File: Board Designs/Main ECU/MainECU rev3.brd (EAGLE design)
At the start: 120.6 x 78.9 mm, 155 parts, among them Q1 MMBT3904LT3G, Q11 MMBT3904LT3G, Q2 MMBT3904LT3G, Q3 MMBT3904LT3G, Q4 MMBT3904LT3G, Q5 MMBT3904LT3G, Q6 MMBT3904LT3G, Q7 MMBT3904LT3G, Q8 MMBT3904LT3G, Q9 MMBT3904LT3G, X1 CONNECTOR-37, X2 CONNECTOR-4AUTOSPORT, X3 CONNECTOR-4NANO-FIT-VERTICAL-4, X4 CONNECTOR-4NANO-FIT-VERTICAL-4

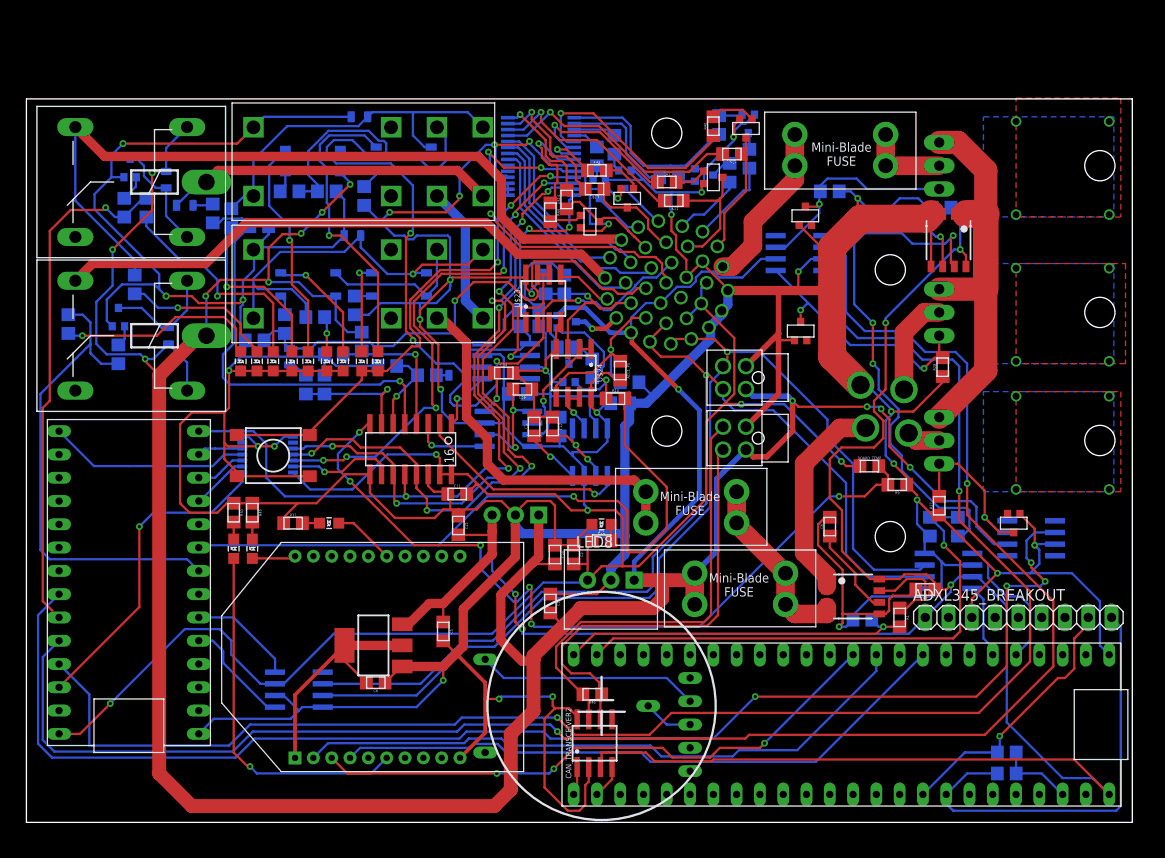
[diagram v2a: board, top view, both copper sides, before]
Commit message: Rename Main ECU rev1b -> rev3, rev3 -> rev4
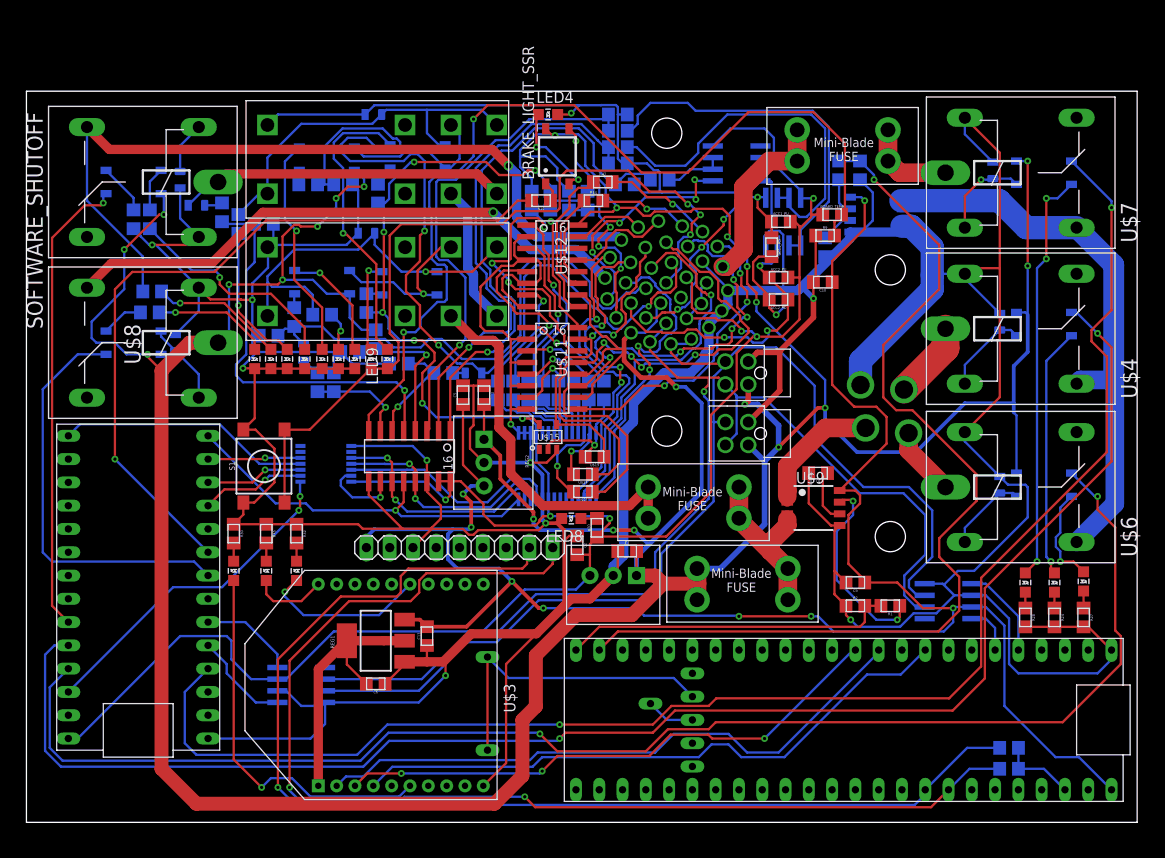
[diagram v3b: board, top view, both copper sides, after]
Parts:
- removed C14, C17: 47pF, HyTechDevices:0805
- removed C15, C16, C18, C19, C21: .1uF, HyTechDevices:0805
- removed C20: .22uF, HyTechDevices:0805
- removed CAN_TRANSCEIVER2: MCP2551, HyTechDevices:SOIC-08
- removed Q1, Q11, Q2, Q3, Q4, Q5, Q6, Q7, Q8, Q9: MMBT3904LT3G, HyTechDevices:SOT23
- removed Q10: (no value), HyTechDevices:SOT23
- removed R46: 120, HyTechDevices:0805
- removed R47, R50: 2.2k, HyTechDevices:0805
- removed R48: 10k, HyTechDevices:0805
- removed R49: 1.2k, HyTechDevices:0805
- removed REG3: 5V, HyTechDevices:OKI-78SR
- removed U$27, U$28: (no value), HyTechDevices:SOIC-08
- added AC1_FILTR, AC2_FILTR: 510, HyTechDevices:0805
- added BRAKE_LIGHT_SSR, FAN_SSR1, FAN_SSR2, INVERTER_SSR, PUMP_SSR: CPC1002N, HyTechDevices:SOP04
- added BR_FILTR: 100, HyTechDevices:0805
- added C13: .1uF, HyTechDevices:0805
- added LED12, LED13, LED16, LED4: Red, HyTechDevices:LED-805
- added R25: 330, HyTechDevices:0805
- added REG2: 5V, HyTechDevices:OKI-78SR
- added U$20, U$21, U$22: JUMPER, HyTechDevices:0805
- C11: value (none) -> .22uF
- C12: value .1uF -> 2.2µ
- C3: value 47pF -> 22µ
- C4: value .1uF -> 22µ
- D7, D8, D9: value MMBZ5246BLT1G -> DIODE0805; device HyTechDevices:SOT23 -> HyTechDevices:0805_D
- R10: value 2.2k -> 43
- R16: value 100 -> 43
- R24, R27, R28: value 10k -> 33
- R35, R36, R38, R39, R40, R41, R42: value 2.2k -> 270
- R37: value 0 -> 270
- R44: value 2.2k -> 0
- U$11, U$12: value JUMPER -> TLP291-4; device HyTechDevices:0805 -> HyTechDevices:SOIC-16
- U$15: value BJT_PNPSOT -> SN74LV1T34; device HyTechDevices:SOT23 -> HyTechDevices:SOT-23-5
- U$16: value CR-2450/G1AN -> JUMPER; device HyTechDevices:CR-2450/G1AN -> HyTechDevices:0805
- U$19: value MC34152 -> JUMPER; device HyTechDevices:SOIC-08 -> HyTechDevices:0805
- U$26: value (none) -> CR-2450/G1AN; device HyTechDevices:SOIC-08 -> HyTechDevices:CR-2450/G1AN
- U$4, U$6, U$7: value N-CHANNEL_MOSFET_FQP30N06L -> G5LE; device HyTechDevices:TO-220-H-HOLE -> HyTechDevices:ZF112
- U$5: value MC34152 -> CPC1002N; device HyTechDevices:SOIC-08 -> HyTechDevices:SOP04
- moved U$5 73.1 mm to (11.7, 69.8), turned to 90 degrees
- moved ADXL345_BREAKOUT 61.4 mm to (46.0, 30.0)
- moved U$16 55.2 mm to (59.2, 67.8), flipped to the bottom, turned to 270 degrees
- moved R24 52.5 mm to (112.1, 22.4), flipped to the top, turned to 270 degrees
- moved U$19 48.4 mm to (62.0, 39.9), flipped to the top, turned to 180 degrees
- moved R3 41.0 mm to (88.6, 71.1)
- moved R4 39.6 mm to (90.9, 71.1)
- moved U$26 38.8 mm to (63.0, 13.0)
- moved R35 37.7 mm to (51.4, 47.1)
- moved C3 35.2 mm to (64.5, 77.2), flipped to the bottom, turned to 180 degrees
- moved U$17 33.8 mm to (57.9, 38.9), turned to 0 degrees
- moved U$13 33.0 mm to (60.7, 36.1)
- moved R40 32.6 mm to (59.7, 47.1), flipped to the bottom
- moved R37 32.4 mm to (54.7, 47.1), turned to 90 degrees
- moved U$14 30.0 mm to (60.7, 38.0), turned to 180 degrees
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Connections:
- removed net DASH_CTRL5_IN: U$12.2, U$17.25
- removed net DASH_CTRL5_OUT: R40.1, U$17.5
- removed net DASH_CTRL6_IN: U$11.2, U$17.26
- removed net DASH_CTRL6_OUT: R41.1, U$17.6
- removed net DASH_CTRL7_IN: U$13.2, U$17.27
- removed net DASH_CTRL7_OUT: R42.1, U$17.7
- removed net DASH_CTRL8_IN: U$14.2, U$17.28
- removed net DASH_CTRL8_OUT: R44.1, U$17.8
- removed net FAN1CONTROL: U$1.A8, U$5.2
- removed net FAN1DRIVE: D8.3, R24.2, U$5.7, U$7.1
- removed net FAN2CONTROL: U$1.A9, U$5.4
- removed net FAN2DRIVE: D7.3, R28.2, U$4.1, U$5.5
- removed net N$66: D4.A, Q9.3, U$8.2
- removed net PUMPCONTROL: U$1.A6, U$19.2
- removed net PUMPDRIVE: D9.3, R27.2, U$19.7, U$6.1
- removed net TELEMETRY_CANH: CAN_TRANSCEIVER2.7, R46.2, X4.P$4
- removed net TELEMETRY_CANL: CAN_TRANSCEIVER2.6, R46.1, X4.P$3
- new net DASH_CTRL5: R39.1, U$17.25
- new net DASH_CTRL6: R40.1, U$13.2, U$17.26
- new net DASH_CTRL7: R41.1, U$14.2, U$17.27
- new net DASH_CTRL8: R42.1, U$15.2, U$17.28, U$19.2
- new net N$20: D8.C, FAN_SSR1.3, U$7.2
- new net N$39: FAN_SSR2.2, LED16.A
- new net N$43: D10.C, R26.1, SOFTWARE_SHUTOFF.2, U$5.3
- new net N$44: R25.2, U$5.2
- new net RELAY_CTRL1: PUMP_SSR.1, U$1.A9
- new net RELAY_CTRL2: FAN_SSR1.1, U$1.D2
- new net RELAY_CTRL3: FAN_SSR2.1, U$1.A8
- net +12V: now also BRAKE_LIGHT_SSR.4, C11.2, FAN_SSR1.4, FAN_SSR2.4, INVERTER_SSR.4, PUMP_SSR.4, REG2.1, U$11.10, U$11.12, U$12.10, U$12.12, U$12.14, U$12.16, U$16.1, U$21.1, U$5.4; no longer C20.2, D10.C, D4.C, R48.1, REG3.1, SOFTWARE_SHUTOFF.2, U$15.2, U$19.6, U$5.6, U$8.1
- net +5V: now also U$15.5, U$20.1, U$22.1; no longer C11.2, C15.1, C18.1, C4.1, U$26.4, U$26.7, U$27.4, U$27.7, U$28.4, U$28.7
- net BRAKE_LIGHT: now also BRAKE_LIGHT_SSR.3; no longer U$15.3
- net CANH: now also X4.P$4
- net CANL: now also X4.P$3
- net CURRENTSENSE2: now also U$4.S, U$6.S, U$7.S; no longer U$4.3, U$6.3, U$7.3
- net DASH_CTRL1: now also U$17.21; no longer U$17.1
- net DASH_CTRL10: now also U$17.2; no longer U$17.22
- net DASH_CTRL11: now also U$17.3; no longer U$17.23
- net DASH_CTRL12: now also U$17.4; no longer U$17.24
- net DASH_CTRL2: now also U$17.22; no longer U$17.2
- net DASH_CTRL3: now also R37.1, U$17.23; no longer R38.1, U$17.3
- net DASH_CTRL4: now also R38.1, U$17.24; no longer R39.1, U$17.4
- net DASH_CTRL9: now also U$17.1; no longer U$17.21
- net DASH_IO2: now also R44.2; no longer R37.2
- net DASH_IO3: now also U$12.13; no longer Q3.3
- net DASH_IO4: now also U$12.15; no longer Q4.3
- net DASH_IO5: now also U$11.9; no longer Q5.3, U$12.1
- net DASH_IO6: now also U$11.11, U$13.1; no longer Q6.3, U$11.1
- net DASH_IO7: now also U$11.13, U$14.1; no longer Q7.3, U$13.1
- net DASH_IO8: now also U$11.15, U$15.4, U$19.1; no longer Q8.3, U$14.1
- net FAN1-: now also U$7.P; no longer U$7.2
- net FAN2-: now also U$4.P; no longer U$4.2
- net GND: now also C13.1, D10.A, D4.A, D7.A, D8.A, D9.A, LED4.C, R24.2, R25.1, R27.2, R28.2, REG2.2, SOFTWARE_SHUTOFF.1, U$11.2, U$11.4, U$11.6, U$11.8, U$12.2, U$12.4, U$12.6, U$12.8, U$15.3, U$4.1, U$6.1, U$7.1, U$8.2; no longer C14.2, C15.2, C16.1, C17.2, C18.2, C19.1, C20.1, C21.1, CAN_TRANSCEIVER2.2, CAN_TRANSCEIVER2.8, D7.1, D8.1, D9.1, Q1.2, Q10.2, Q11.2, Q2.2, Q3.2, Q4.2, Q5.2, Q6.2, Q7.2, Q8.2, Q9.2, R24.1, R27.1, R28.1, REG3.2, U$19.3, U$25.7, U$26.3, U$27.3, U$28.3, U$5.3
- net INVERTER_CTRL: now also INVERTER_SSR.1; no longer R16.1, R47.1
- net N$17: now also BRAKE_LIGHT_SSR.1, R10.1; no longer Q10.3, R48.2, R49.1
- net N$21: now also D9.C, FAN_SSR2.3, U$4.2; no longer C3.1, U$27.8
- net N$23: now also AC2_FILTR.1; no longer U$28.2
- net N$24: now also AC1_FILTR.1; no longer U$27.2
- net N$25: now also BR_FILTR.1; no longer U$26.2
- net N$26: now also D4.C, INVERTER_SSR.3, U$8.1; no longer Q11.1, R50.2
- net N$27: now also INVERTER_SSR.2, R16.1; no longer D10.A, Q11.3, SOFTWARE_SHUTOFF.1
- net N$30: now also LED16.C, R24.1; no longer Q2.1, R36.2
- net N$36: now also LED13.C, R28.1; no longer C16.2, U$28.1, U$28.6
- net N$37: now also LED12.C, R27.1; no longer C19.2, U$26.1, U$26.6
- net N$38: now also LED12.A, PUMP_SSR.2; no longer C14.1, U$28.8
- net N$4: now also D7.C, PUMP_SSR.3, U$6.2; no longer C12.2, U$27.1, U$27.6
- net N$41: now also U$2.3.3V_2, U$26.+_0, U$26.+_1; no longer C17.1, U$26.8
- net N$42: now also FAN_SSR1.2, LED13.A; no longer Q2.3, R37.1
- net N$51: now also U$12.7; no longer Q1.1
- net N$52: now also R36.2, U$12.5; no longer Q3.1, R38.2
- net N$53: now also R37.2, U$12.3; no longer Q4.1, R39.2
- net N$54: now also R38.2, U$12.1; no longer Q5.1, R40.2
- net N$55: now also R39.2, U$11.7; no longer Q6.1, R41.2
- net N$56: now also R40.2, U$11.5; no longer Q7.1, R42.2
- net N$57: now also R41.2, U$11.3; no longer Q8.1, R44.2
- net N$58: now also R42.2, U$11.1; no longer R49.2, U$15.1
- net N$59: now also U$12.9; no longer Q1.3
- net N$60: now also R44.1, U$12.11; no longer U$16.+_0, U$16.+_1, U$2.3.3V_2
- net N$61: now also U$11.16, U$16.2, U$20.2; no longer U$16.-, U$2.GND_2
- net N$62: now also U$11.14, U$21.2, U$22.2; no longer CAN_TRANSCEIVER2.4, U$2.A15
- net N$64: now also U$2.GND_2, U$26.-; no longer CAN_TRANSCEIVER2.1, U$2.A14
- net N$65: now also U$25.7; no longer Q9.1, R47.2
- net N$7: now also BRAKE_LIGHT_SSR.2, LED4.A; no longer Q10.1, R10.1
- net PUMP1-: now also U$6.P; no longer U$6.2
- net READ_ACCEL1: now also AC1_FILTR.2, C4.1; no longer U$27.5
- net READ_ACCEL2: now also AC2_FILTR.2, C3.1; no longer U$28.5
- net READ_BRAKE: now also BR_FILTR.2, C12.2; no longer U$26.5
- net SOFTWARE_SHUTDOWN: now also U$5.1; no longer R26.1, R50.1
- net TELEMETRY5V: now also C13.2, REG2.3; no longer C21.2, CAN_TRANSCEIVER2.3, REG3.3
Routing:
- net FAN1CONTROL: track 188.9 -> 0.00 mm, vias 2 -> 0
- net FAN2CONTROL: track 174.9 -> 0.00 mm, vias 2 -> 0
- net RELAY_CTRL3: track 0.00 -> 168.4 mm, vias 0 -> 2
- net RELAY_CTRL2: track 0.00 -> 164.8 mm, vias 0 -> 2
- net RELAY_CTRL1: track 0.00 -> 156.2 mm, vias 0 -> 2
- net PUMPCONTROL: track 150.2 -> 0.00 mm, vias 4 -> 0
- net +12V: track 381.7 -> 488.8 mm, vias 13 -> 22
- net SDA: track 29.3 -> 130.8 mm
- net SCL: track 48.1 -> 130.1 mm, vias 0 -> 2
- net +5V: track 337.4 -> 284.2 mm, vias 14 -> 13
- net READ_BRAKE: track 6.70 -> 59.5 mm
- net N$6: track 56.2 -> 4.00 mm, vias 3 -> 0
- net SCK_5V: track 75.2 -> 25.9 mm, vias 6 -> 2
- net TELEMETRY_CANH: track 48.8 -> 0.00 mm
- net COOLINGSENSE: track 57.5 -> 106.3 mm
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- removed copper zone on layer 1, net HEATSINK_FAN1
- removed copper zone on layer 16, net HEATSINK_FAN1
- removed copper zone on layer 1, net HEATSINK_FAN2
- removed copper zone on layer 16, net HEATSINK_FAN2
- removed copper zone on layer 1, net HEATSINK_PUMP1
- removed copper zone on layer 16, net HEATSINK_PUMP1
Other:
- board size 120.6 x 78.9 mm -> 121.2 x 79.8 mm
- board text added: "Designed By Parker Jones"
- board text added: "Fan1"
- board text added: "Fan2"
- board text added: "HyTech 2019 Main ECU rev1b"
- board text added: "PUMP"
- board text removed: "Designed by Parker Jones"
- board text removed: "HyTech 2019 Main ECU rev3"
- board text removed: "Shutdown Latch"
- board text removed: "Updates by Nathan Cheek"
- board text removed: "↑FAN1"
- board text removed: "↑PUMP1"
- board text removed: "↓FAN2"

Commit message: Main ECU rev3/4: Update silkscreen for manufacturing, Main ECU rev4: switch to high-side dashboard switching and flip parts on wrong side
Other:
- board text added: "HyTech 2019 Main ECU rev3"
- board text removed: "HyTech 2019 Main ECU rev1b"
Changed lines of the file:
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@@
 <wire x1="121.158" y1="79.756" x2="0" y2="79.756" width="0" layer="20"/>
 <wire x1="0" y1="79.756" x2="0" y2="0" width="0" layer="20"/>
-<text x="1.778" y="4.572" size="1.3208" layer="51" font="vector">HyTech 2019 Main ECU rev1b</text>
+<text x="1.778" y="4.572" size="1.3208" layer="51" font="vector">HyTech 2019 Main ECU rev3</text>
 <text x="1.778" y="2.032" size="1.3208" layer="51" font="vector">Designed By Parker Jones</text>
 <text x="25.146" y="26.162" size="0.8128" layer="51" rot="R90">MQTT</text>

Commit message: Main ECU rev{1-4}: Add warning about RTC cell assembly, specify current sensor input capacitor value, lower XBee LED resistor to 33R; Main ECU rev{2,4}: Specify MCP3208 input capacitor value; Main ECU rev4: Lower relay-controlling transistors' base resistor to 1k; Main ECU rev5: make all relevant changes previously listed
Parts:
- C10, C9: value (none) -> 0.1uF
- R45: value 2.3k -> 33
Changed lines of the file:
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@@
 <attribute name="VALUE" x="65.532" y="28.8798" size="0.3048" layer="27" align="top-center"/>
 </element>
-<element name="C10" library="HyTechDevices" package="0805" value="" x="86.868" y="58.928" smashed="yes" rot="R180">
+<element name="C10" library="HyTechDevices" package="0805" value="0.1uF" x="86.868" y="58.928" smashed="yes" rot="R180">
 <attribute name="NAME" x="86.868" y="58.2041" size="0.3048" layer="25" rot="R180" align="bottom-center"/>
 <attribute name="VALUE" x="86.868" y="59.6392" size="0.3048" layer="27" rot="R180" align="top-center"/>
@@
 <attribute name="VALUE" x="86.36" y="38.8112" size="0.3048" layer="27" rot="R180" align="top-center"/>
 </element>
-<element name="C9" library="HyTechDevices" package="0805" value="" x="90.424" y="26.162" smashed="yes" rot="R180">
+<element name="C9" library="HyTechDevices" package="0805" value="0.1uF" x="90.424" y="26.162" smashed="yes" rot="R180">
 <attribute name="NAME" x="90.424" y="25.4381" size="0.3048" layer="25" rot="R180" align="bottom-center"/>
 <attribute name="VALUE" x="90.424" y="26.8732" size="0.3048" layer="27" rot="R180" align="top-center"/>
@@
 <attribute name="VALUE" x="61.849" y="67.1068" size="0.3048" layer="27" align="top-center"/>
 </element>
-<element name="R45" library="HyTechDevices" package="0805" value="2.3k" x="26.162" y="31.496" smashed="yes" rot="R270">
+<element name="R45" library="HyTechDevices" package="0805" value="33" x="26.162" y="31.496" smashed="yes" rot="R270">
 <attribute name="NAME" x="26.8859" y="31.496" size="0.3048" layer="25" rot="R270" align="bottom-center"/>
 <attribute name="VALUE" x="25.4508" y="31.496" size="0.3048" layer="27" rot="R270" align="top-center"/>

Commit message: Main ECU rev{1-5}: Update values of LED resistors based on testing
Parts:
- R11: value 43 -> 150
- R14, R21: value 820 -> 2k
- R17: value 820 -> 20k
- R31: value 1.2K -> 6.8k
- R32: value 100 -> 1.2k
- R45: value 33 -> 0
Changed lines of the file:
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@@
 <attribute name="VALUE" x="56.134" y="68.5292" size="0.3048" layer="27" rot="R180" align="top-center"/>
 </element>
-<element name="R11" library="HyTechDevices" package="0805" value="43" x="30.734" y="69.596" smashed="yes" rot="MR180">
+<element name="R11" library="HyTechDevices" package="0805" value="150" x="30.734" y="69.596" smashed="yes" rot="MR180">
 <attribute name="NAME" x="30.734" y="68.8721" size="0.3048" layer="26" rot="MR180" align="bottom-center"/>
 <attribute name="VALUE" x="30.734" y="70.3072" size="0.3048" layer="28" rot="MR180" align="top-center"/>
@@
 <attribute name="VALUE" x="37.6428" y="68.58" size="0.3048" layer="28" rot="MR90" align="top-center"/>
 </element>
-<element name="R14" library="HyTechDevices" package="0805" value="820" x="32.258" y="55.372" smashed="yes" rot="MR180">
+<element name="R14" library="HyTechDevices" package="0805" value="2k" x="32.258" y="55.372" smashed="yes" rot="MR180">
 <attribute name="NAME" x="32.258" y="54.6481" size="0.3048" layer="26" rot="MR180" align="bottom-center"/>
 <attribute name="VALUE" x="32.258" y="56.0832" size="0.3048" layer="28" rot="MR180" align="top-center"/>
@@
 <attribute name="VALUE" x="13.462" y="56.3372" size="0.3048" layer="28" rot="MR180" align="top-center"/>
 </element>
-<element name="R17" library="HyTechDevices" package="0805" value="820" x="23.114" y="65.278" smashed="yes" rot="MR270">
+<element name="R17" library="HyTechDevices" package="0805" value="20k" x="23.114" y="65.278" smashed="yes" rot="MR270">
 <attribute name="NAME" x="22.3901" y="65.278" size="0.3048" layer="26" rot="MR270" align="bottom-center"/>
 <attribute name="VALUE" x="23.8252" y="65.278" size="0.3048" layer="28" rot="MR270" align="top-center"/>
@@
 <attribute name="VALUE" x="62.9412" y="32.131" size="0.3048" layer="27" rot="R90" align="top-center"/>
 </element>
-<element name="R21" library="HyTechDevices" package="0805" value="820" x="29.21" y="55.118" smashed="yes" rot="MR90">
+<element name="R21" library="HyTechDevices" package="0805" value="2k" x="29.21" y="55.118" smashed="yes" rot="MR90">
 <attribute name="NAME" x="29.9339" y="55.118" size="0.3048" layer="26" rot="MR90" align="bottom-center"/>
 <attribute name="VALUE" x="28.4988" y="55.118" size="0.3048" layer="28" rot="MR90" align="top-center"/>
@@
 <attribute name="VALUE" x="21.8948" y="31.496" size="0.3048" layer="27" rot="R270" align="top-center"/>
 </element>
-<element name="R31" library="HyTechDevices" package="0805" value="1.2K" x="13.716" y="57.912" smashed="yes" rot="MR180">
+<element name="R31" library="HyTechDevices" package="0805" value="6.8k" x="13.716" y="57.912" smashed="yes" rot="MR180">
 <attribute name="NAME" x="13.716" y="57.1881" size="0.3048" layer="26" rot="MR180" align="bottom-center"/>
 <attribute name="VALUE" x="13.716" y="58.6232" size="0.3048" layer="28" rot="MR180" align="top-center"/>
 </element>
-<element name="R32" library="HyTechDevices" package="0805" value="100" x="29.464" y="31.496" smashed="yes" rot="R270">
+<element name="R32" library="HyTechDevices" package="0805" value="1.2k" x="29.464" y="31.496" smashed="yes" rot="R270">
 <attribute name="NAME" x="30.1879" y="31.496" size="0.3048" layer="25" rot="R270" align="bottom-center"/>
 <attribute name="VALUE" x="28.7528" y="31.496" size="0.3048" layer="27" rot="R270" align="top-center"/>
@@
 <attribute name="VALUE" x="61.849" y="67.1068" size="0.3048" layer="27" align="top-center"/>
 </element>
-<element name="R45" library="HyTechDevices" package="0805" value="33" x="26.162" y="31.496" smashed="yes" rot="R270">
+<element name="R45" library="HyTechDevices" package="0805" value="0" x="26.162" y="31.496" smashed="yes" rot="R270">
 <attribute name="NAME" x="26.8859" y="31.496" size="0.3048" layer="25" rot="R270" align="bottom-center"/>
 <attribute name="VALUE" x="25.4508" y="31.496" size="0.3048" layer="27" rot="R270" align="top-center"/>

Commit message: Main ECU rev{1-5}: Update values of OKI-78SR capacitors to 10uF
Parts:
- C1, C11: value .22uF -> 10uF
- C13, C2: value .1uF -> 10uF
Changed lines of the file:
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@@
 <attribute name="VALUE" x="69.088" y="69.3928" size="0.3048" layer="28" rot="MR0" align="top-center"/>
 </element>
-<element name="C1" library="HyTechDevices" package="0805" value=".22uF" x="65.532" y="29.591" smashed="yes">
+<element name="C1" library="HyTechDevices" package="0805" value="10uF" x="65.532" y="29.591" smashed="yes">
 <attribute name="NAME" x="65.532" y="30.3149" size="0.3048" layer="25" align="bottom-center"/>
 <attribute name="VALUE" x="65.532" y="28.8798" size="0.3048" layer="27" align="top-center"/>
@@
 <attribute name="VALUE" x="86.868" y="59.6392" size="0.3048" layer="27" rot="R180" align="top-center"/>
 </element>
-<element name="C11" library="HyTechDevices" package="0805" value=".22uF" x="49.911" y="46.609" smashed="yes" rot="R270">
+<element name="C11" library="HyTechDevices" package="0805" value="10uF" x="49.911" y="46.609" smashed="yes" rot="R270">
 <attribute name="NAME" x="50.6349" y="46.609" size="0.3048" layer="25" rot="R270" align="bottom-center"/>
 <attribute name="VALUE" x="49.1998" y="46.609" size="0.3048" layer="27" rot="R270" align="top-center"/>
@@
 <attribute name="VALUE" x="65.278" y="68.8848" size="0.3048" layer="28" rot="MR0" align="top-center"/>
 </element>
-<element name="C13" library="HyTechDevices" package="0805" value=".1uF" x="43.688" y="20.32" smashed="yes" rot="R90">
+<element name="C13" library="HyTechDevices" package="0805" value="10uF" x="43.688" y="20.32" smashed="yes" rot="R90">
 <attribute name="NAME" x="42.9641" y="20.32" size="0.3048" layer="25" rot="R90" align="bottom-center"/>
 <attribute name="VALUE" x="44.3992" y="20.32" size="0.3048" layer="27" rot="R90" align="top-center"/>
 </element>
-<element name="C2" library="HyTechDevices" package="0805" value=".1uF" x="60.071" y="30.226" smashed="yes" rot="R270">
+<element name="C2" library="HyTechDevices" package="0805" value="10uF" x="60.071" y="30.226" smashed="yes" rot="R270">
 <attribute name="NAME" x="60.7949" y="30.226" size="0.3048" layer="25" rot="R270" align="bottom-center"/>
 <attribute name="VALUE" x="59.3598" y="30.226" size="0.3048" layer="27" rot="R270" align="top-center"/>
